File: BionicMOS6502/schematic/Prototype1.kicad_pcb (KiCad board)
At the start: 2 copper layers, 48.3 x 71.1 mm, 11 parts, among them J1 BionicConnector, U1 W65C816S, U2 74HC126

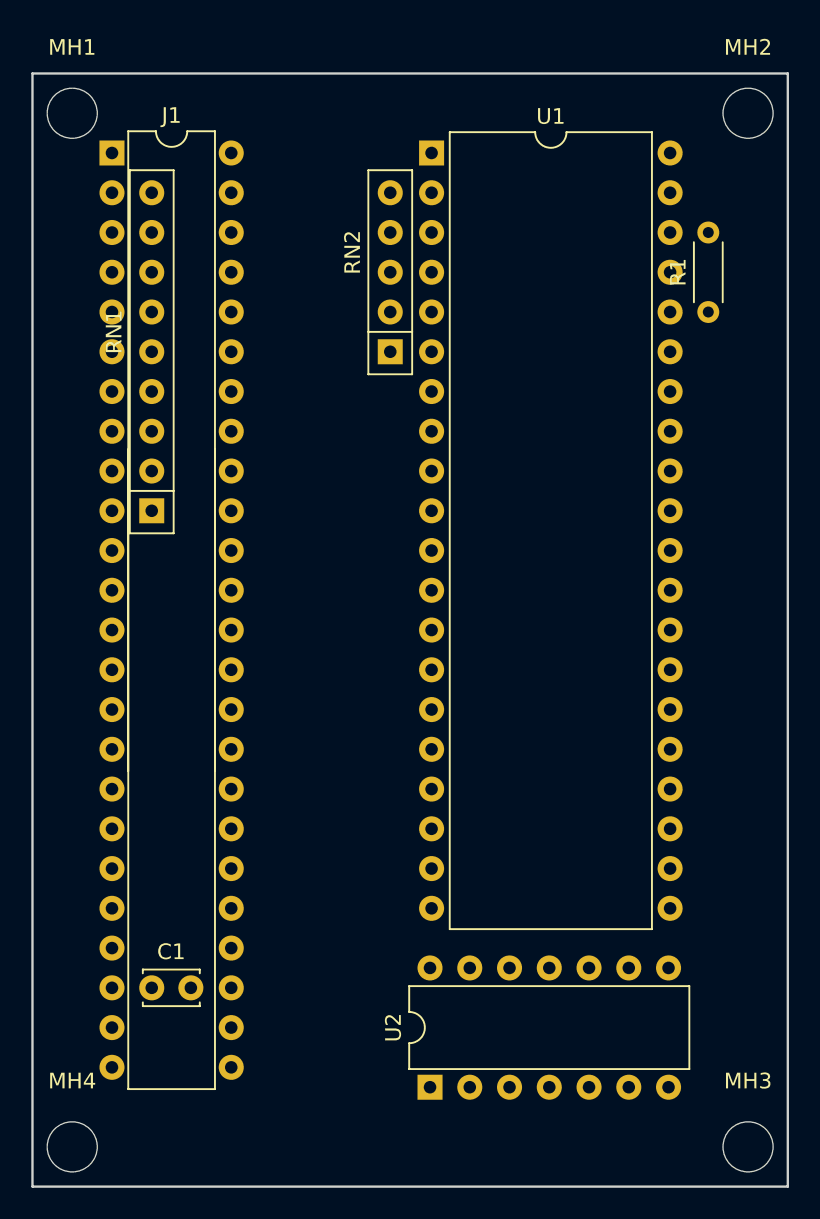
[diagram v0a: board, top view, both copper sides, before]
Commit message: [BionicMOS6502] Add bypass capaciters to prevent sprious #NMI
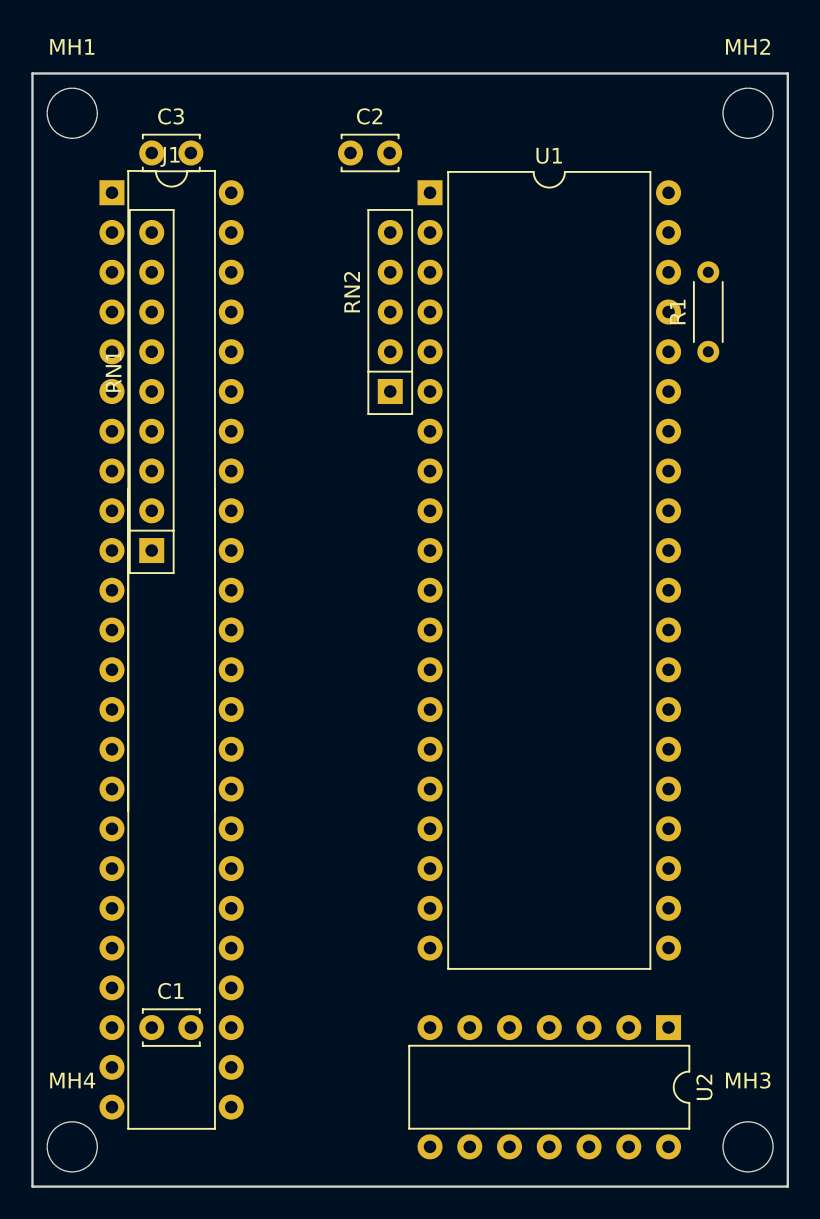
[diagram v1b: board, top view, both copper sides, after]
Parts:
- added C2: 0.1u, Capacitor_THT:C_Disc_D3.4mm_W2.1mm_P2.50mm, F.Cu at (118.8, 72.5)
- added C3: 0.1u, Capacitor_THT:C_Disc_D3.4mm_W2.1mm_P2.50mm, F.Cu at (106.1, 72.5)
- moved U2 15.7 mm to (139.1, 128.4), turned to 270 degrees
- moved U1 2.54 mm to (123.9, 75.1)
- moved RN2 2.54 mm to (121.3, 87.8)
- moved C1 2.54 mm to (106.1, 128.4)
- moved J1 2.54 mm to (103.5, 75.1)
- moved R1 2.54 mm to (141.6, 85.2)
- moved RN1 2.54 mm to (106.1, 97.9)

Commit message: Fix Bionic connector pin outs
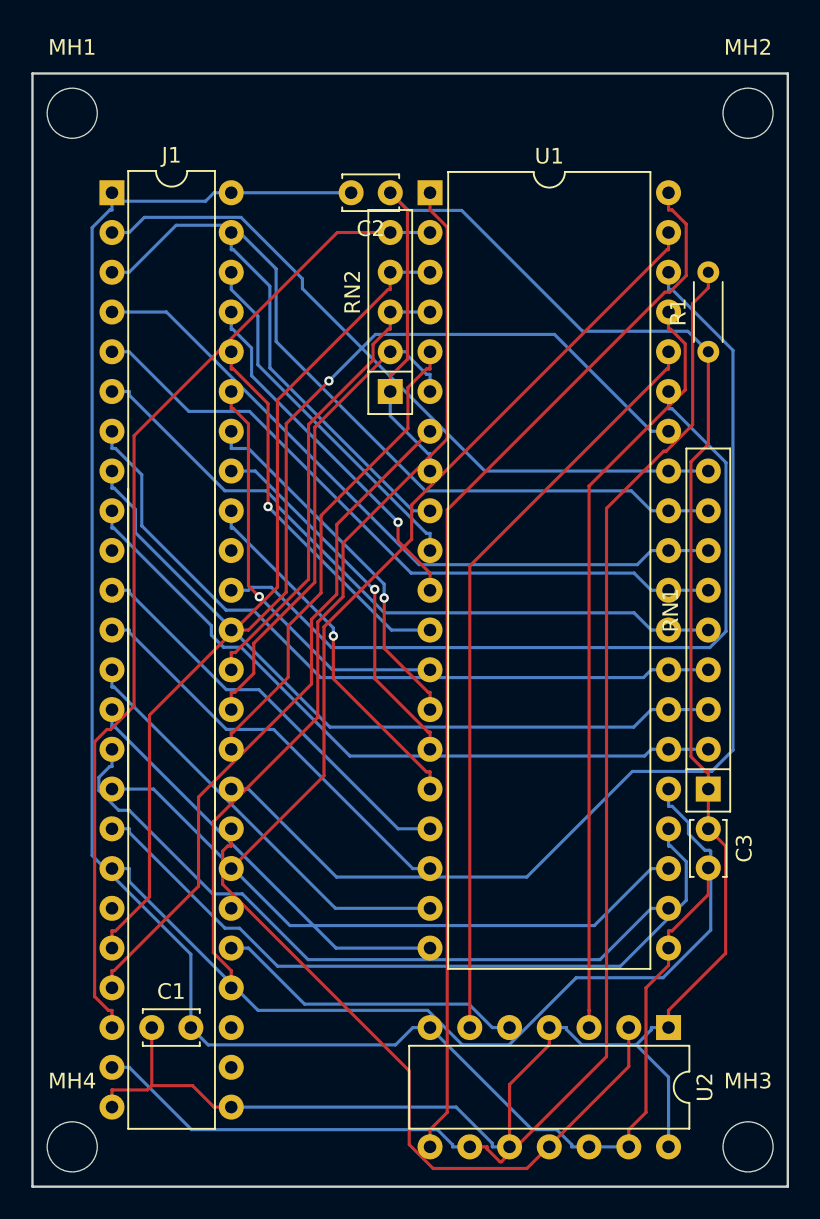
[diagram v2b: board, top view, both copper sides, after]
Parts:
- moved C3 55.9 mm to (141.6, 115.7), turned to 270 degrees
- moved RN1 38.7 mm to (141.6, 113.2)
- moved C2 3.59 mm to (121.3, 75.1), turned to 180 degrees
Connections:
- J1 pad 11: /P20 -> /P30
- J1 pad 12: /P21 -> /P31
- J1 pad 13: /P22 -> /P32
- J1 pad 14: /P23 -> /P33
- J1 pad 15: /P24 -> /P34
- J1 pad 16: /P25 -> /P35
- J1 pad 17: /P26 -> /P36
- J1 pad 18: /P27 -> /P37
- J1 pad 40: /P37 -> /P27
- J1 pad 41: /P36 -> /P26
- J1 pad 42: /P35 -> /P25
- J1 pad 43: /P34 -> /P24
- J1 pad 44: /P33 -> /P23
- J1 pad 45: /P32 -> /P22
- J1 pad 46: /P31 -> /P21
- J1 pad 47: /P30 -> /P20
- R1 pad 2: /P45 -> /P53
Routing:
- net VCC: track 0.00 -> 147.4 mm
- net GND: track 0.00 -> 124.3 mm
- net /P53: track 0.00 -> 89.9 mm
- net /P45: track 0.00 -> 70.1 mm
- net Net-(U1-Pad40): track 0.00 -> 68.5 mm
- net /P52: track 0.00 -> 63.9 mm
- net /P55: track 0.00 -> 57.9 mm
- net /P37: track 0.00 -> 56.9 mm
- net /P50: track 0.00 -> 53.3 mm
- net /P47: track 0.00 -> 52.3 mm
- net /P40: track 0.00 -> 50.7 mm
- net /P11: track 0.00 -> 49.6 mm
- net Net-(U1-Pad37): track 0.00 -> 48.8 mm
- net Net-(U1-Pad36): track 0.00 -> 48.5 mm
- net /P15: track 0.00 -> 47.4 mm
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
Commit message: Migrate to KiCad 6.0
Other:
- net class Default removed
